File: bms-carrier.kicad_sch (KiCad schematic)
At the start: 1 part, among them J1 1-746610-7

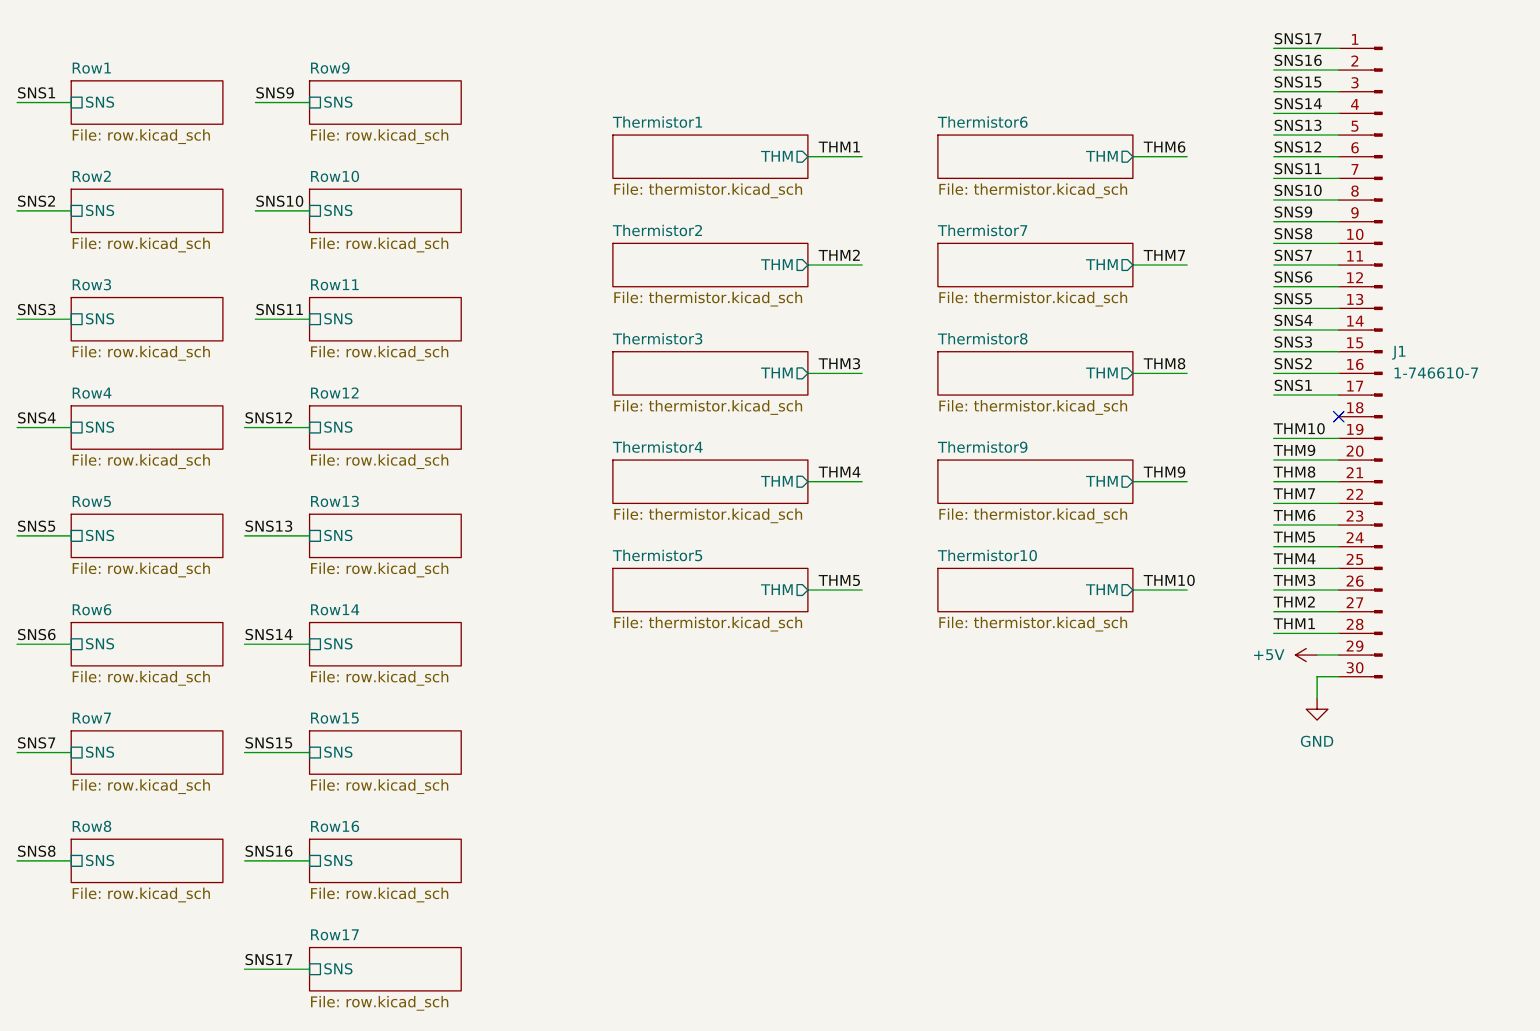
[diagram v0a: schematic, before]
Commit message: Change last end to 0 from 17
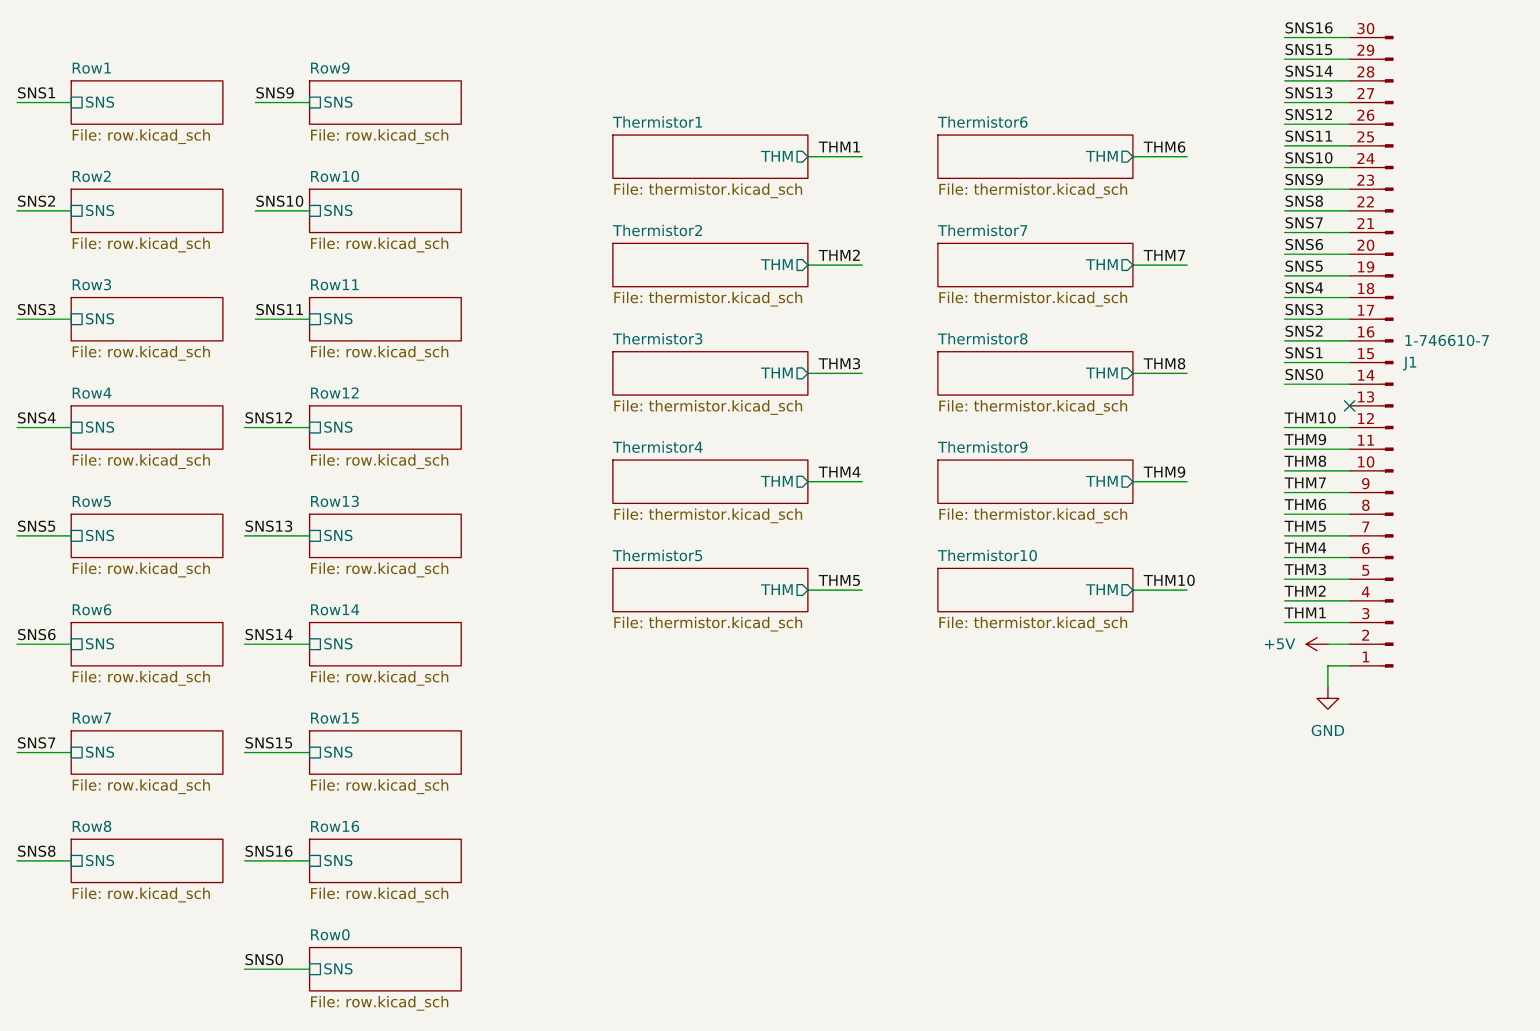
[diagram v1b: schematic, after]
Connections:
- net SNS17 is gone; now on net GND: J1.1 (Pin_1)
- net +5V: now also J1.2 (Pin_2); no longer J1.29 (Pin_29)
- net GND: no longer J1.30 (Pin_30)
- net SNS1: now also J1.15 (Pin_15); no longer J1.17 (Pin_17)
- net SNS10: now also J1.24 (Pin_24); no longer J1.8 (Pin_8)
- net SNS11: now also J1.25 (Pin_25); no longer J1.7 (Pin_7)
- net SNS12: now also J1.26 (Pin_26); no longer J1.6 (Pin_6)
- net SNS13: now also J1.27 (Pin_27); no longer J1.5 (Pin_5)
- net SNS14: now also J1.28 (Pin_28); no longer J1.4 (Pin_4)
- net SNS15: now also J1.29 (Pin_29); no longer J1.3 (Pin_3)
- net SNS16: now also J1.30 (Pin_30); no longer J1.2 (Pin_2)
- net SNS3: now also J1.17 (Pin_17); no longer J1.15 (Pin_15)
- net SNS4: now also J1.18 (Pin_18); no longer J1.14 (Pin_14)
- net SNS5: now also J1.19 (Pin_19); no longer J1.13 (Pin_13)
- net SNS6: now also J1.20 (Pin_20); no longer J1.12 (Pin_12)
- net SNS7: now also J1.21 (Pin_21); no longer J1.11 (Pin_11)
- net SNS8: now also J1.22 (Pin_22); no longer J1.10 (Pin_10)
- net SNS9: now also J1.23 (Pin_23); no longer J1.9 (Pin_9)
- net THM1: now also J1.3 (Pin_3); no longer J1.28 (Pin_28)
- net THM10: now also J1.12 (Pin_12); no longer J1.19 (Pin_19)
- net THM2: now also J1.4 (Pin_4); no longer J1.27 (Pin_27)
- net THM3: now also J1.5 (Pin_5); no longer J1.26 (Pin_26)
- net THM4: now also J1.6 (Pin_6); no longer J1.25 (Pin_25)
- net THM5: now also J1.7 (Pin_7); no longer J1.24 (Pin_24)
- net THM6: now also J1.8 (Pin_8); no longer J1.23 (Pin_23)
- net THM7: now also J1.9 (Pin_9); no longer J1.22 (Pin_22)
- net THM8: now also J1.10 (Pin_10); no longer J1.21 (Pin_21)
- net THM9: now also J1.11 (Pin_11); no longer J1.20 (Pin_20)
- new net SNS0: J1.14 (Pin_14)
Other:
- sheet Row17 renamed Row0
- moved on the sheet: J1
